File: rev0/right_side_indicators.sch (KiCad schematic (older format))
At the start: 1 part, among them IC1 ECP5-BGA256

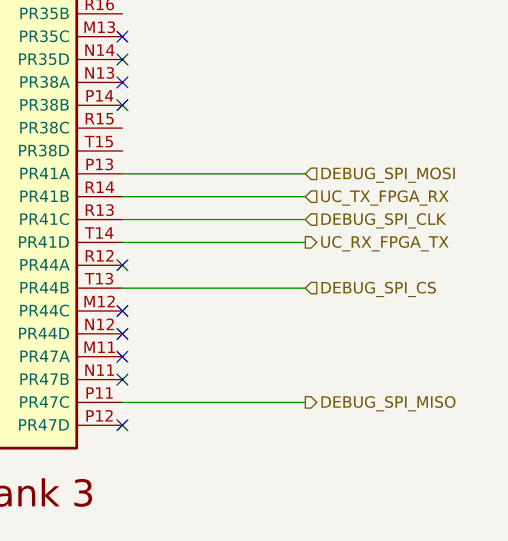
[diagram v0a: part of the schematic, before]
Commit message: hardware: adopt OSHWA convention for SPI signal names
https://www.oshwa.org/a-resolution-to-redefine-spi-signal-names
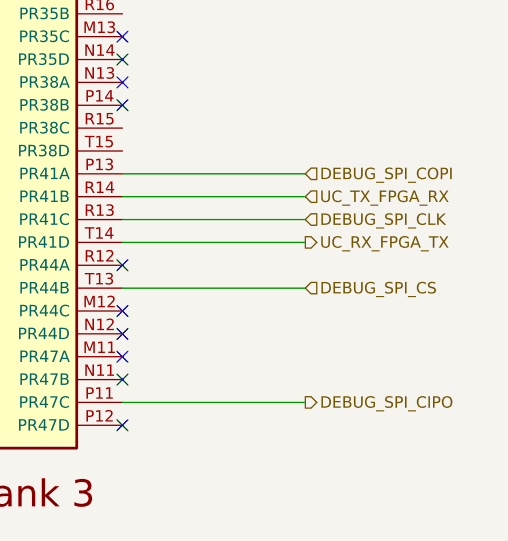
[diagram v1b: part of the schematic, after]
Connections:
- net DEBUG_SPI_MISO renamed DEBUG_SPI_CIPO
- net DEBUG_SPI_MOSI renamed DEBUG_SPI_COPI
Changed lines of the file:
@@
 	3150 4400 3950 4400
 Text HLabel 3950 5400 2    50   Output ~ 0
-DEBUG_SPI_MISO
+DEBUG_SPI_CIPO
 Text HLabel 3950 4600 2    50   Input ~ 0
 DEBUG_SPI_CLK
 Text HLabel 3950 4400 2    50   Input ~ 0
-DEBUG_SPI_MOSI
+DEBUG_SPI_COPI
 Text HLabel 3950 4900 2    50   Input ~ 0
 DEBUG_SPI_CS

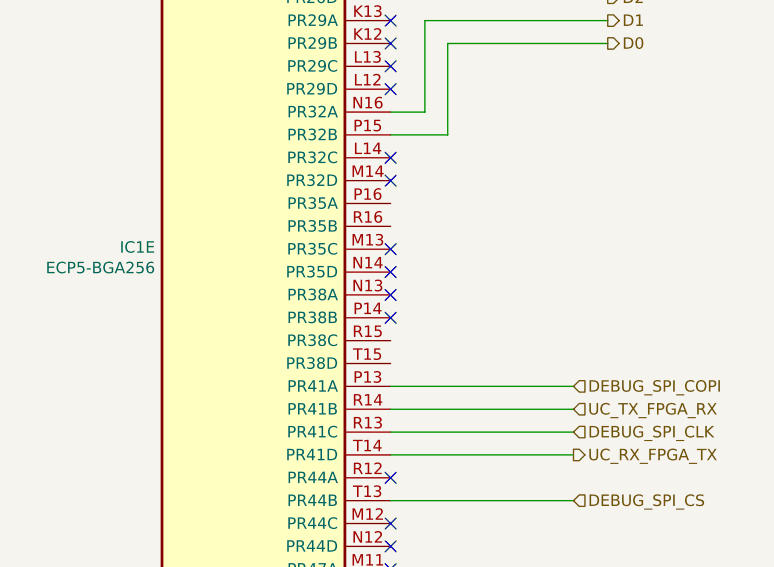
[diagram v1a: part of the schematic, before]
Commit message: hardware: replace U6 ATSAMD21 with ATSAMD11
remove FORCE_RECOVERY button
renumber button references
remove FPGA connections to U6 and replace with test points:
    CS_DI
    FPGA_CONFIG_CLK
    FPGA_DONE
    FPGA_INIT
    DEBUG_SPI_MISO
    DEBUG_SPI_MOSI
    DEBUG_SPI_CLK
    DEBUG_SPI_CS
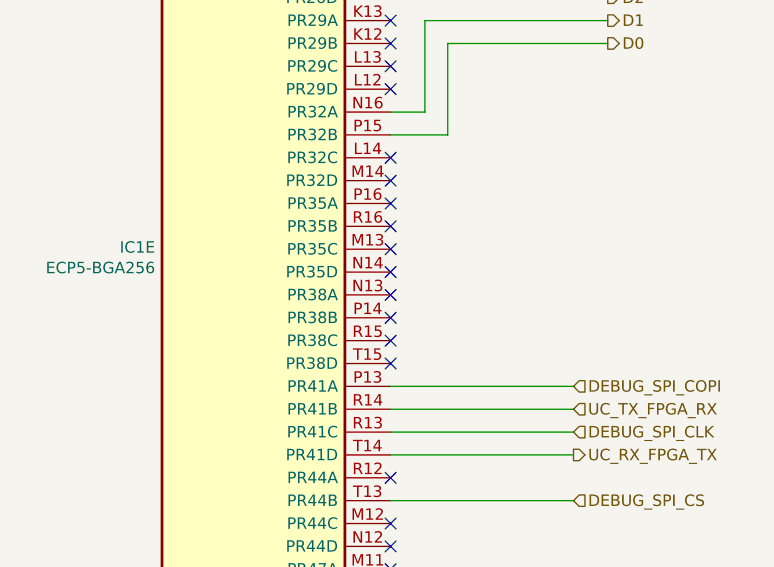
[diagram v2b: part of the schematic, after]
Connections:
- no-connect marks 16 -> 20
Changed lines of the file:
@@
 Wire Wire Line
 	3150 4600 3950 4600
+NoConn ~ 3150 3600
+NoConn ~ 3150 4200
+NoConn ~ 3150 3700
+NoConn ~ 3150 4300
 $EndSCHEMATC

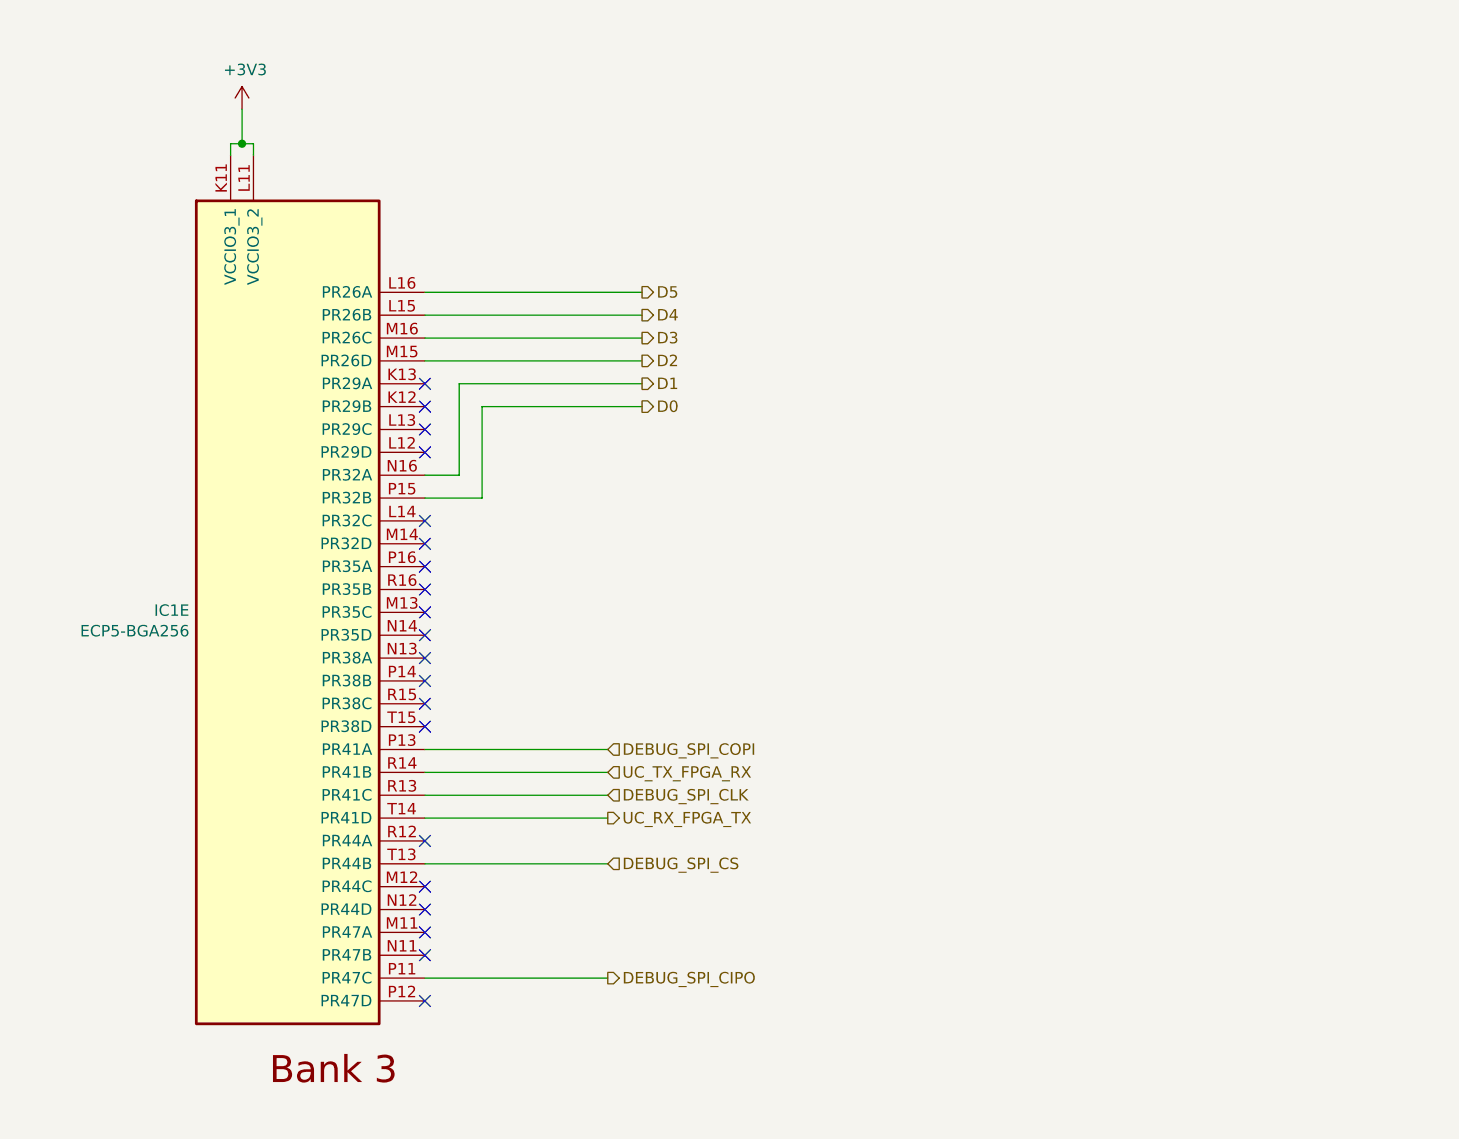
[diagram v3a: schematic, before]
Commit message: hardware: change micro USB connectors to Type-C (J1, J2, J4)
Thanks for the footprint, Glasgow!
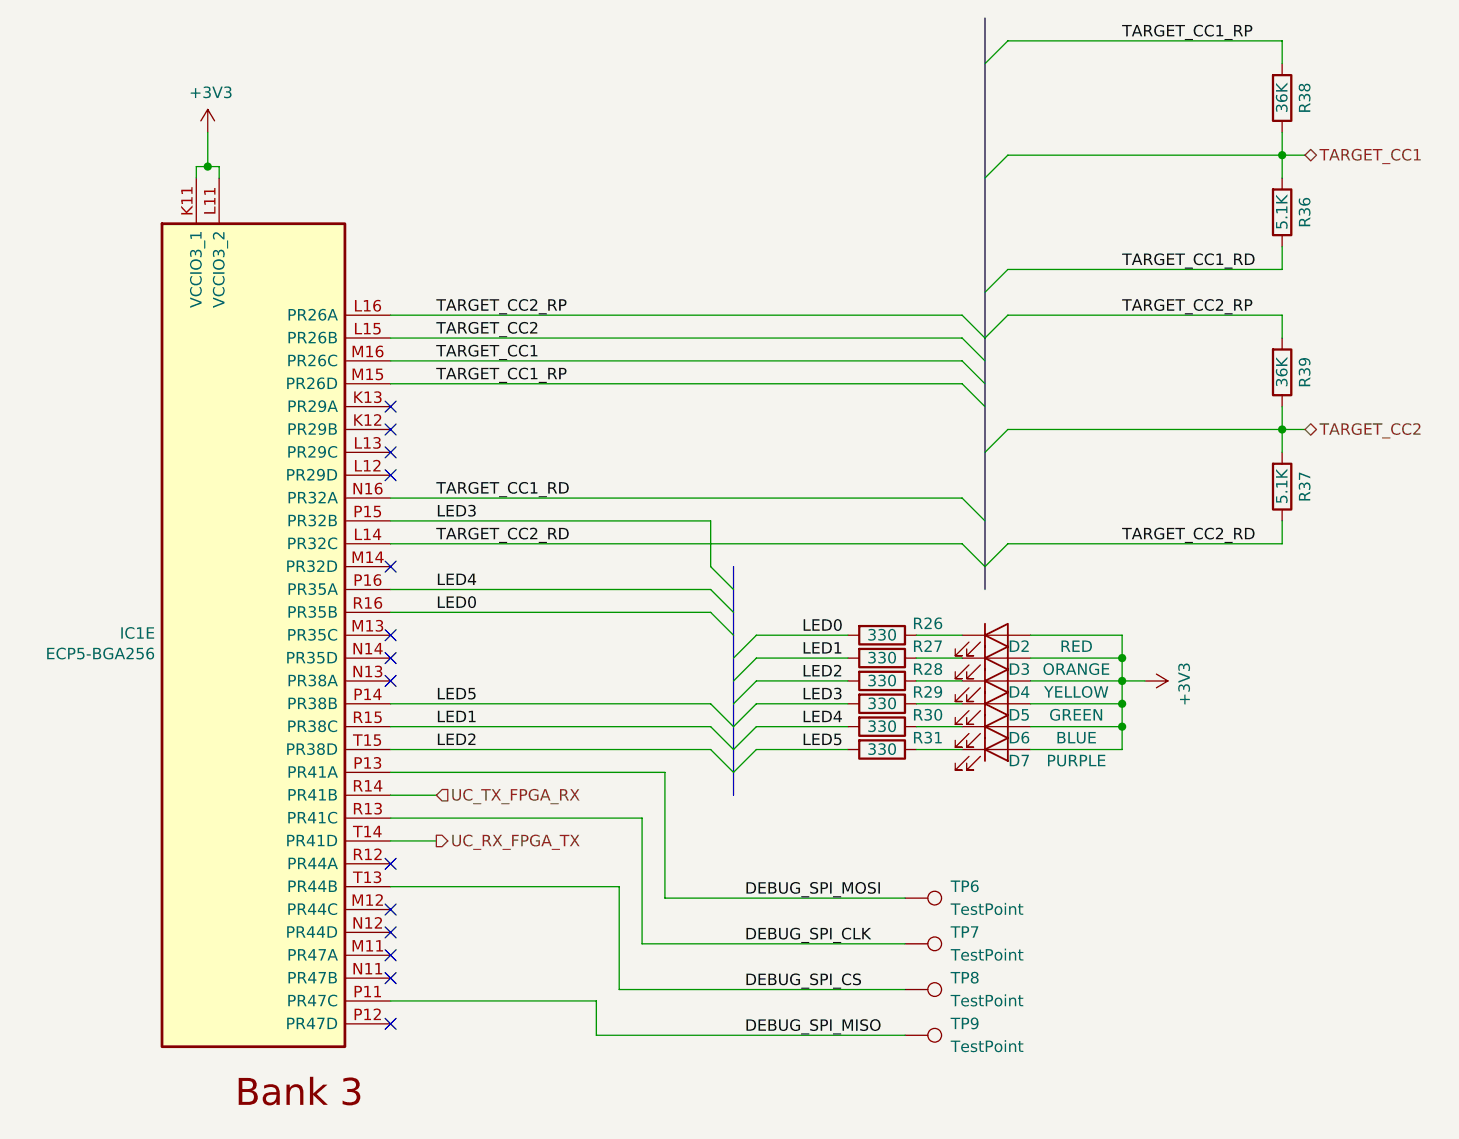
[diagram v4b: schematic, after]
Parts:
- added D2: RED, LED_SMD:LED_0603_1608Metric_Pad1.05x0.95mm_HandSolder, symbol Device:LED
- added D3: ORANGE, LED_SMD:LED_0603_1608Metric_Pad1.05x0.95mm_HandSolder, symbol Device:LED
- added D4: YELLOW, LED_SMD:LED_0603_1608Metric_Pad1.05x0.95mm_HandSolder, symbol Device:LED
- added D5: GREEN, LED_SMD:LED_0603_1608Metric_Pad1.05x0.95mm_HandSolder, symbol Device:LED
- added D6: BLUE, LED_SMD:LED_0603_1608Metric_Pad1.05x0.95mm_HandSolder, symbol Device:LED
- added D7: PURPLE, LED_SMD:LED_0603_1608Metric_Pad1.05x0.95mm_HandSolder, symbol Device:LED
- added R26, R27, R28, R29, R30, R31: 330, Resistor_SMD:R_0402_1005Metric, symbol Device:R
- added R36, R37: 5.1K, Resistor_SMD:R_0402_1005Metric, symbol Device:R
- added R38, R39: 36K, Resistor_SMD:R_0402_1005Metric, symbol Device:R
- added TP6, TP7, TP8, TP9: TestPoint, TestPoint:TestPoint_Pad_D1.0mm, symbol Connector:TestPoint
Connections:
- net +3V3: now also D2.2 (A), D3.2 (A), D4.2 (A), D5.2 (A), D6.2 (A), D7.2 (A)
- net DEBUG_SPI_CLK: now also TP7.1
- net DEBUG_SPI_CS: now also TP8.1
- net TARGET_CC2_RD: now reaches IC1.L14 (PR32C)
- net TARGET_CC2_RD: now also R37.1
- net LED5: now reaches IC1.P14 (PR38B)
- net LED5: now also R31.2
- net LED4: now reaches IC1.P16 (PR35A)
- net LED4: now also R30.2
- net LED1: now reaches IC1.R15 (PR38C)
- net LED1: now also R27.2
- net LED0: now reaches IC1.R16 (PR35B)
- net LED0: now also R26.2
- net LED2: now reaches IC1.T15 (PR38D)
- net LED2: now also R28.2
- net D0 renamed LED3
- net LED3: now also R29.2
- net D1 renamed TARGET_CC1_RD
- net TARGET_CC1_RD: now also R36.1
- net D2 renamed TARGET_CC1_RP
- net TARGET_CC1_RP: now also R38.2
- net D3 renamed TARGET_CC1
- net TARGET_CC1: now also R36.2, R38.1
- net D4 renamed TARGET_CC2
- net TARGET_CC2: now also R37.2, R39.1
- net D5 renamed TARGET_CC2_RP
- net TARGET_CC2_RP: now also R39.2
- net DEBUG_SPI_CIPO renamed DEBUG_SPI_MISO
- net DEBUG_SPI_MISO: now also TP9.1
- net DEBUG_SPI_COPI renamed DEBUG_SPI_MOSI
- net DEBUG_SPI_MOSI: now also TP6.1
- new net: D2.1 (K), R26.1
- new net: D3.1 (K), R27.1
- new net: D4.1 (K), R28.1
- new net: D5.1 (K), R29.1
- new net: D6.1 (K), R30.1
- new net: D7.1 (K), R31.1
- no-connect marks 20 -> 14
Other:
- moved on the sheet: IC1E

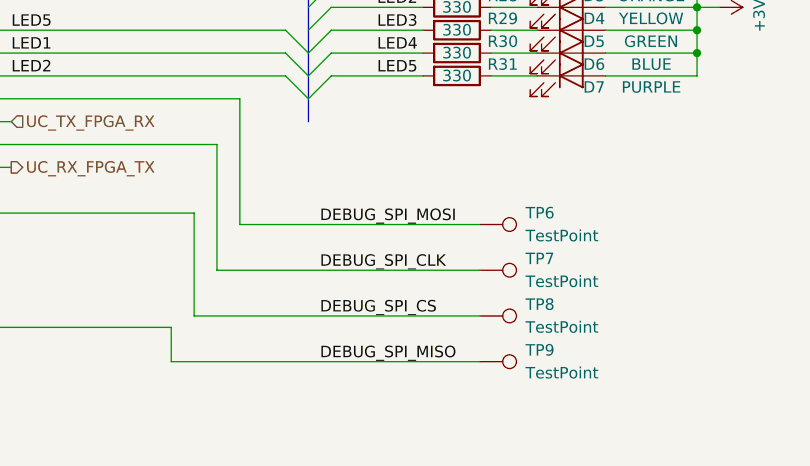
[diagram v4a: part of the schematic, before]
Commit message: hardware: adopt OSHWA convention for SPI signal names
https://www.oshwa.org/a-resolution-to-redefine-spi-signal-names
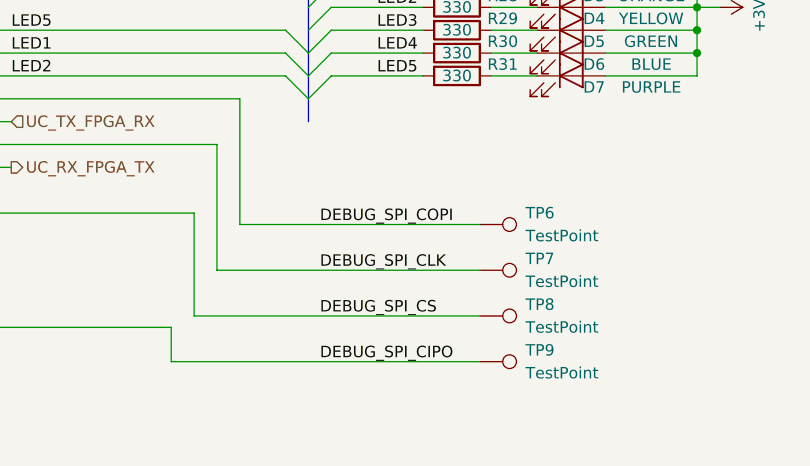
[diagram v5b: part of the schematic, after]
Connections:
- net DEBUG_SPI_MISO renamed DEBUG_SPI_CIPO
- net DEBUG_SPI_MOSI renamed DEBUG_SPI_COPI
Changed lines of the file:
@@
 DEBUG_SPI_CS
 Text Label 4550 5650 0    50   ~ 0
-DEBUG_SPI_MISO
+DEBUG_SPI_CIPO
 Text Label 4550 5250 0    50   ~ 0
 DEBUG_SPI_CLK
 Text Label 4550 5050 0    50   ~ 0
-DEBUG_SPI_MOSI
+DEBUG_SPI_COPI
 Wire Wire Line
 	3000 4500 4200 4500

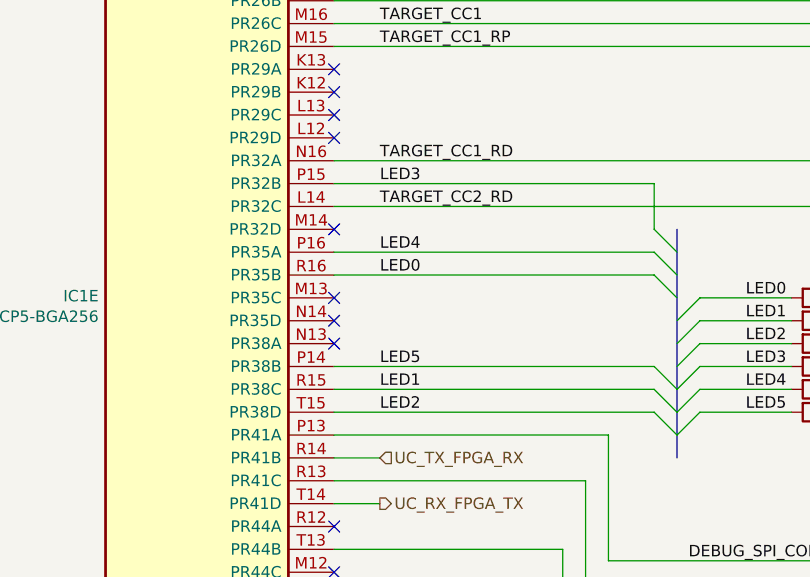
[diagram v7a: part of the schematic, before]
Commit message: hardware: shrink board outline to 48x48 mm
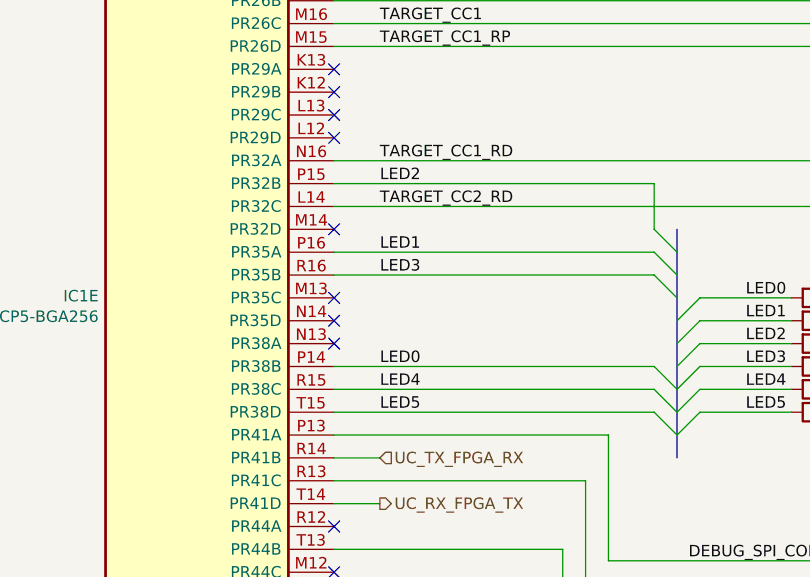
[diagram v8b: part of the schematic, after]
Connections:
- net LED0: now also IC1.P14 (PR38B); no longer IC1.R16 (PR35B)
- net LED1: now also IC1.P16 (PR35A); no longer IC1.R15 (PR38C)
- net LED2: now also IC1.P15 (PR32B); no longer IC1.T15 (PR38D)
- net LED3: now also IC1.R16 (PR35B); no longer IC1.P15 (PR32B)
- net LED4: now also IC1.R15 (PR38C); no longer IC1.P16 (PR35A)
- net LED5: now also IC1.T15 (PR38D); no longer IC1.P14 (PR38B)
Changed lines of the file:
@@
 Wire Wire Line
 	3000 4300 4400 4300
-Text Label 3200 3400 0    50   ~ 0
+Text Label 3200 3800 0    50   ~ 0
 LED3
+Text Label 3200 4300 0    50   ~ 0
+LED4
+Text Label 3200 4400 0    50   ~ 0
+LED5
 Text Label 3200 3700 0    50   ~ 0
-LED4
-Text Label 3200 4200 0    50   ~ 0
-LED5
-Text Label 3200 4300 0    50   ~ 0
 LED1
 Entry Wire Line
@@
 Wire Wire Line
 	3900 5650 3900 5500
-Text Label 3200 3800 0    50   ~ 0
+Text Label 3200 4200 0    50   ~ 0
 LED0
-Text Label 3200 4400 0    50   ~ 0
+Text Label 3200 3400 0    50   ~ 0
 LED2
-Wire Bus Line
-	5600 1200 5600 3700
-Wire Bus Line
-	4500 3600 4500 4600
 $Comp
 L Connector:TestPoint TP?
@@
 	0    1    -1   0
 $EndComp
+Wire Bus Line
+	5600 1200 5600 3700
+Wire Bus Line
+	4500 3600 4500 4600
 $EndSCHEMATC
